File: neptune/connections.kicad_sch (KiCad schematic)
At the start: 6 parts, among them J1 Conn_01x02, J4 USB_B_Micro, J5 Conn_01x04, J6 Conn_01x04, J7 Conn_01x04, U6 USBLC6-2SC6

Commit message: Updated some footprints, restarted routing
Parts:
- J5: footprint Connector_JST:JST_EH_B4B-EH-A_1x04_P2.50mm_Vertical -> Connector_PinHeader_2.54mm:PinHeader_1x04_P2.54mm_Vertical
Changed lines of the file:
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@@
       (effects (font (size 1.27 1.27)) (justify left))
     )
-    (property "Footprint" "Connector_JST:JST_EH_B4B-EH-A_1x04_P2.50mm_Vertical" (at 49.53 82.55 0)
+    (property "Footprint" "Connector_PinHeader_2.54mm:PinHeader_1x04_P2.54mm_Vertical" (at 49.53 82.55 0)
       (effects (font (size 1.27 1.27)) hide)
     )

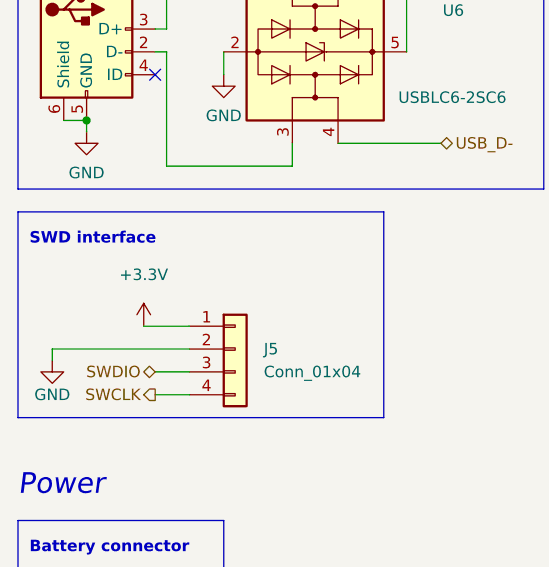
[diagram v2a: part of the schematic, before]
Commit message: Routed 3.3V stepdown, added indicator LEDs
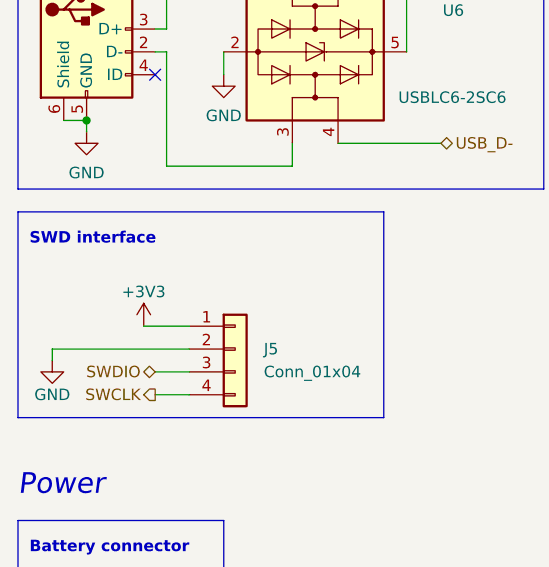
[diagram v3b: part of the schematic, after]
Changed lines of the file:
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@@
-    )
-  )
-  (symbol (lib_id "power:+3.3V") (at 39.37 80.01 0) (unit 1)
-    (in_bom yes) (on_board yes) (dnp no) (fields_autoplaced)
-    (property "Reference" "#PWR041" (at 39.37 83.82 0)
-      (effects (font (size 1.27 1.27)) hide)
-    )
-    (property "Value" "+3.3V" (at 39.37 74.295 0)
-      (effects (font (size 1.27 1.27)))
-    )
-    (property "Footprint" "" (at 39.37 80.01 0)
-      (effects (font (size 1.27 1.27)) hide)
-    )
-    (property "Datasheet" "" (at 39.37 80.01 0)
-      (effects (font (size 1.27 1.27)) hide)
-    )
-    (pin "1")
-    (instances
-      (project "neptune"
-        (path "/e63e39d7-6ac0-4ffd-8aa3-1841a4541b55/708c8a34-f258-4554-8b50-7818f1e46fec"
-          (reference "#PWR041") (unit 1)
-        )
-        (path "/e63e39d7-6ac0-4ffd-8aa3-1841a4541b55/ecfbb819-cfce-4fa1-8e12-b36915786c58"
-          (reference "#PWR068") (unit 1)
-        )
-      )
     )
   )
@@
         )
       )
+    )
+  )
+  (symbol (lib_id "power:+3V3") (at 39.37 80.01 0) (unit 1)
+    (in_bom yes) (on_board yes) (dnp no) (fields_autoplaced)
+    (property "Reference" "#PWR04" (at 39.37 83.82 0)
+      (effects (font (size 1.27 1.27)) hide)
+    )
+    (property "Value" "+3V3" (at 39.37 76.2 0)
+      (effects (font (size 1.27 1.27)))
+    )
+    (property "Footprint" "" (at 39.37 80.01 0)
+      (effects (font (size 1.27 1.27)) hide)
+    )
+    (property "Datasheet" "" (at 39.37 80.01 0)
+      (effects (font (size 1.27 1.27)) hide)
+    )
+    (pin "1")
+    (instances
+      (project "neptune"
+        (path "/e63e39d7-6ac0-4ffd-8aa3-1841a4541b55/761c8e29-382a-475c-a37a-7201cc9cd0f5"
+          (reference "#PWR04") (unit 1)
+        )
+        (path "/e63e39d7-6ac0-4ffd-8aa3-1841a4541b55/ecfbb819-cfce-4fa1-8e12-b36915786c58"
+          (reference "#PWR045") (unit 1)
+        )
+      )
